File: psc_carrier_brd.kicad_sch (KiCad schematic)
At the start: 9 parts, among them J1 1731130154, J2 0836149012, J5 39301022, J6 6469028-1

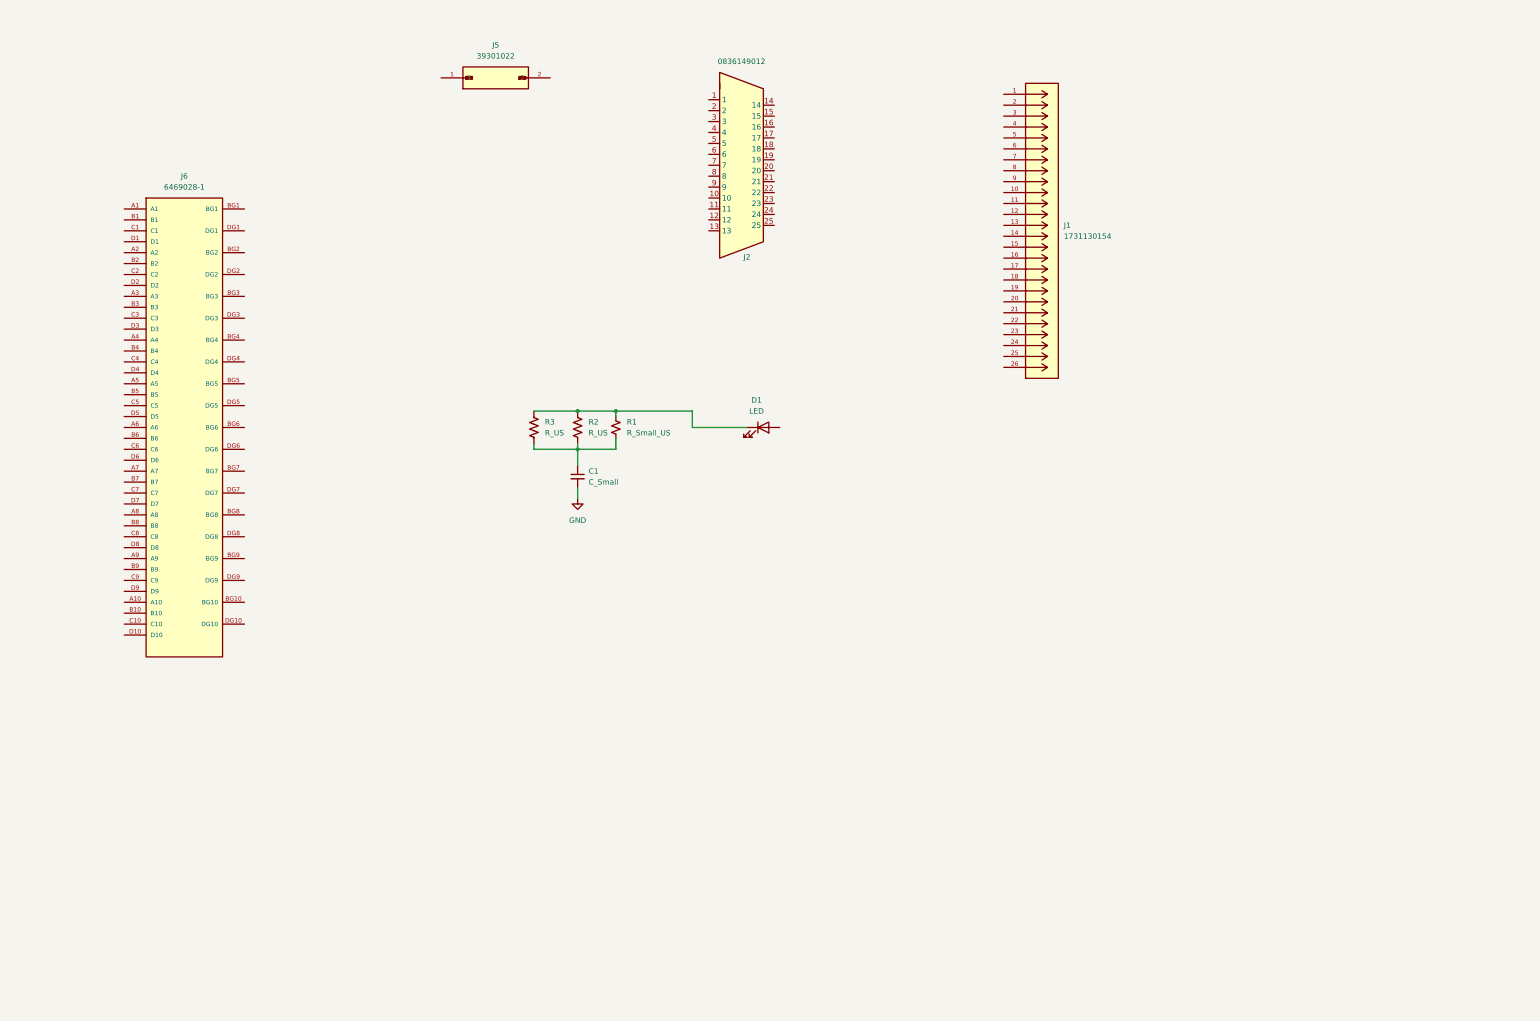
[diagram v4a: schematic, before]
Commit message: Upgrade to KiCad 9.  Add all I/O connectors
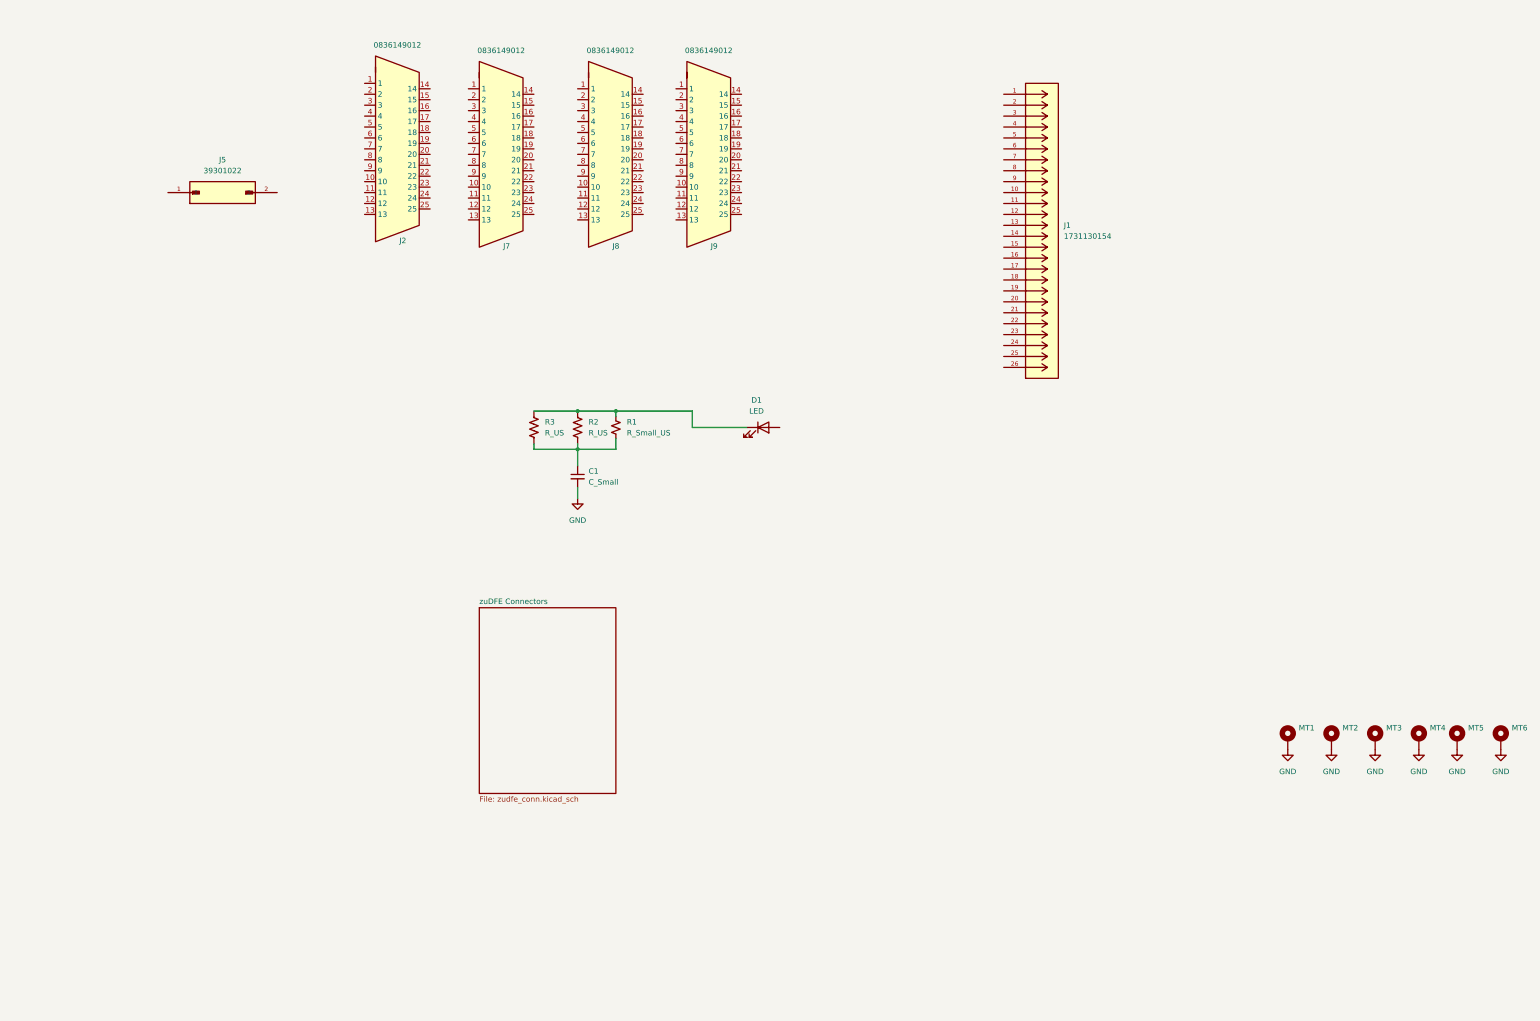
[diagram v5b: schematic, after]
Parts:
- removed J6: 6469028-1, myparts:TE_6469028-1, symbol 6469028-1:6469028-1
- added J7, J8, J9: 0836149012, myparts:0836149012, symbol 0836149012:0836149012
- added MT1, MT2, MT3, MT4, MT5, MT6: MountingHole_Pad, MountingHole:MountingHole_4.3mm_M4_DIN965_Pad, symbol Mechanical:MountingHole_Pad
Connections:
- net GND: now also MT1.1, MT2.1, MT3.1, MT4.1, MT5.1, MT6.1
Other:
- added sheet zuDFE Connectors (zudfe_conn.kicad_sch)
- moved on the sheet: J2, J5

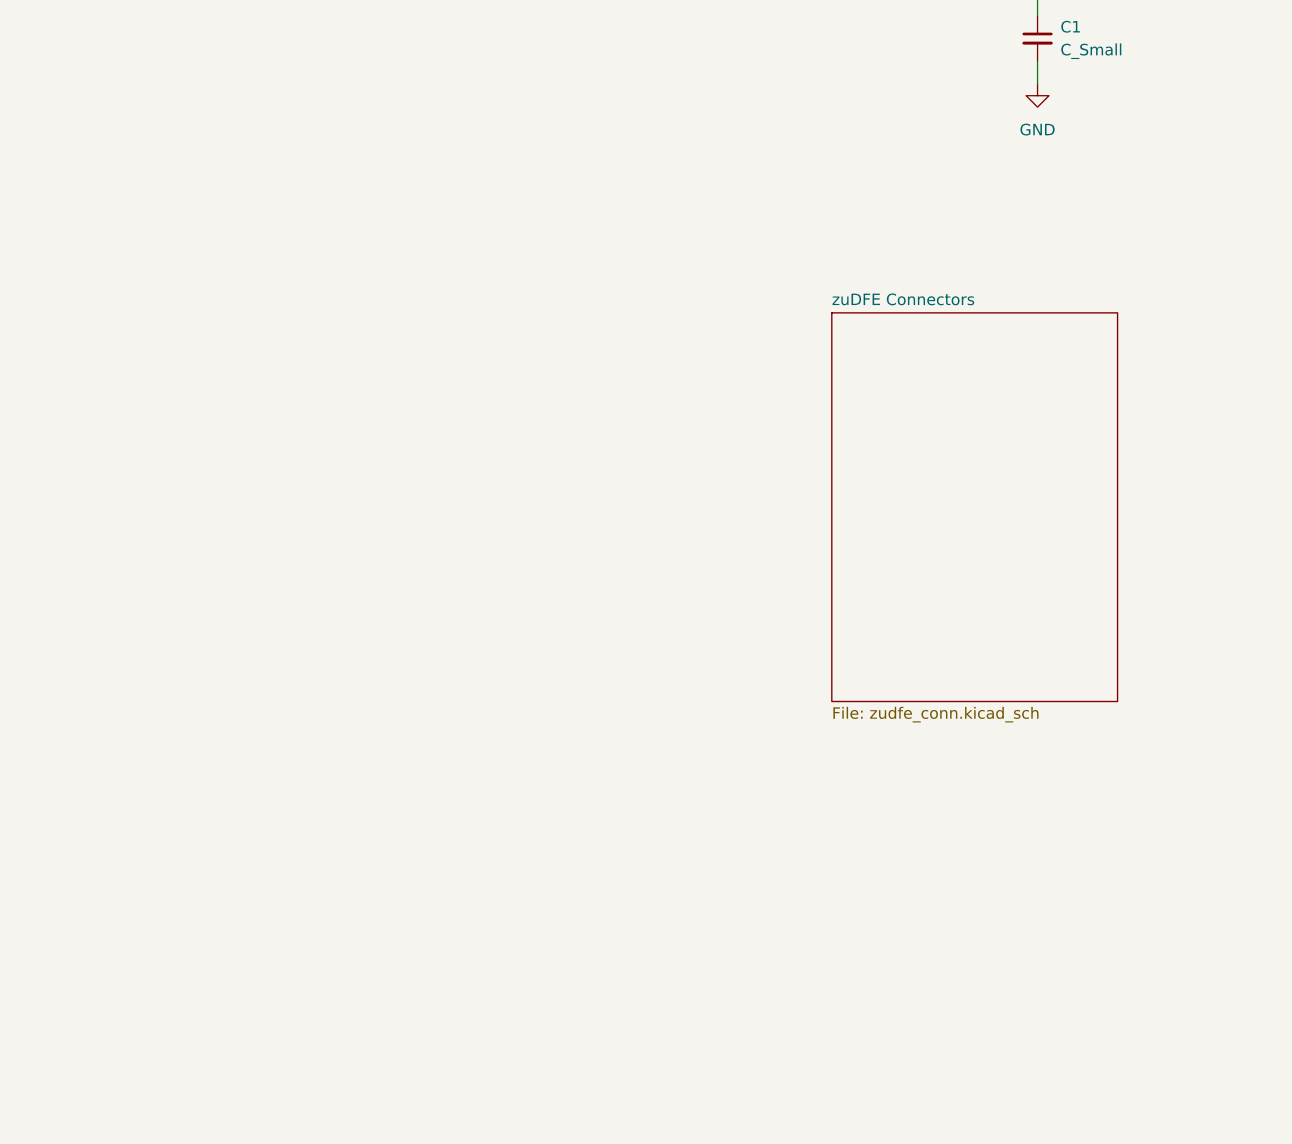
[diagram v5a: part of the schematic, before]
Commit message: Add DAC schematic page
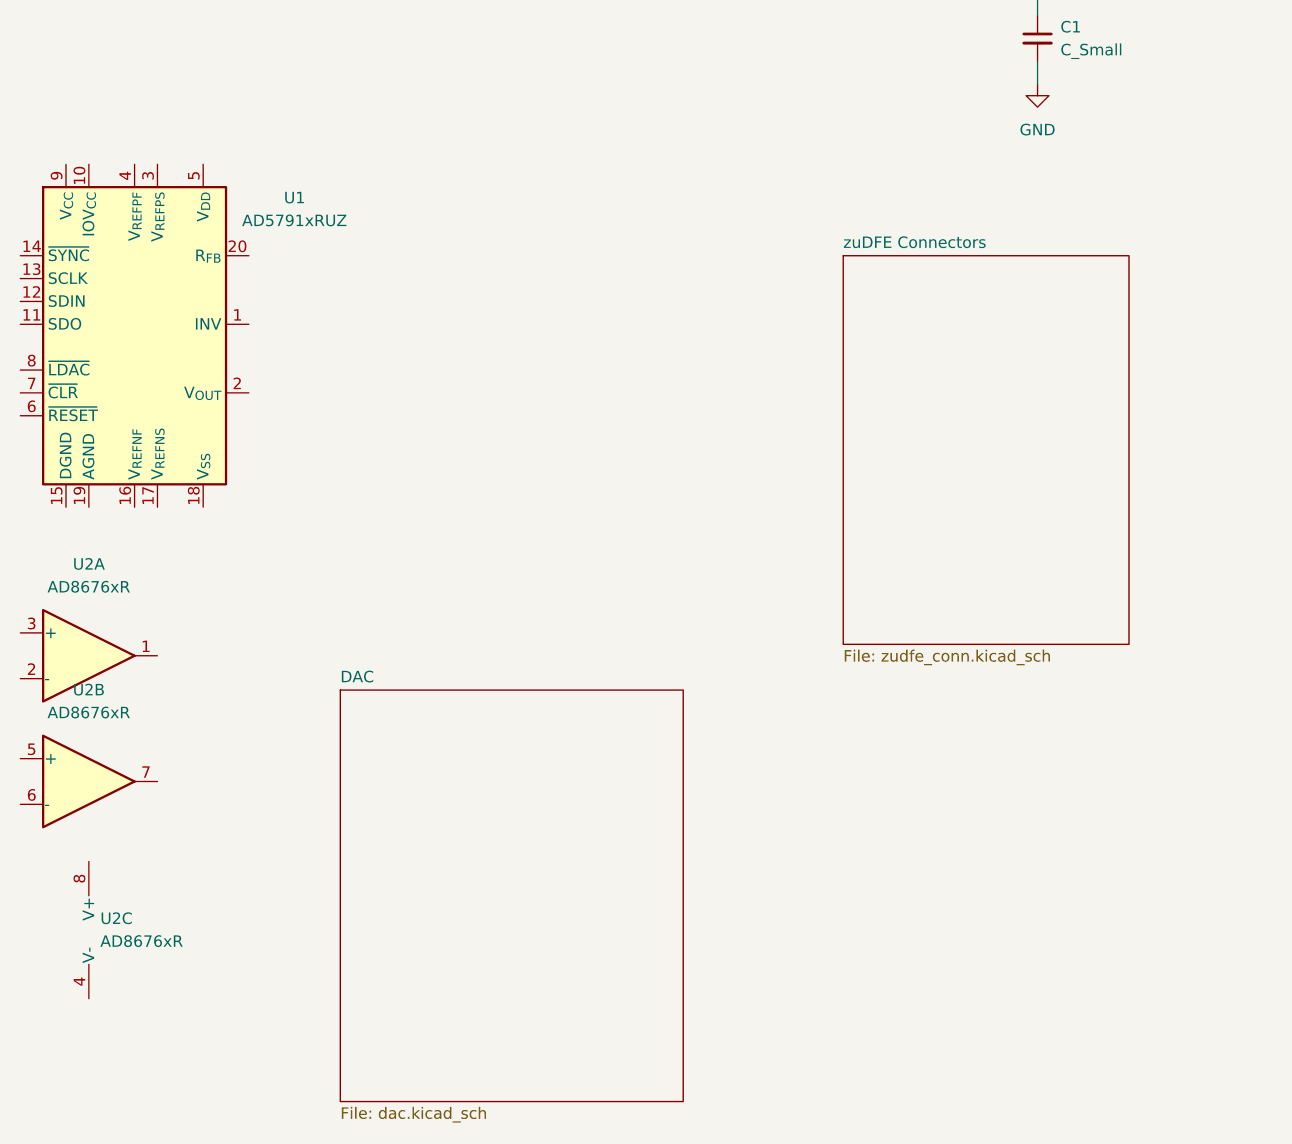
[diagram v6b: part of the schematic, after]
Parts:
- added U1: AD5791xRUZ, Package_SO:TSSOP-20_4.4x6.5mm_P0.65mm, symbol Analog_DAC:AD5791xRUZ
- added U2: AD8676xR, Package_SO:SOIC-8_3.9x4.9mm_P1.27mm, symbol Amplifier_Operational:AD8676xR
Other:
- added sheet DAC (dac.kicad_sch)

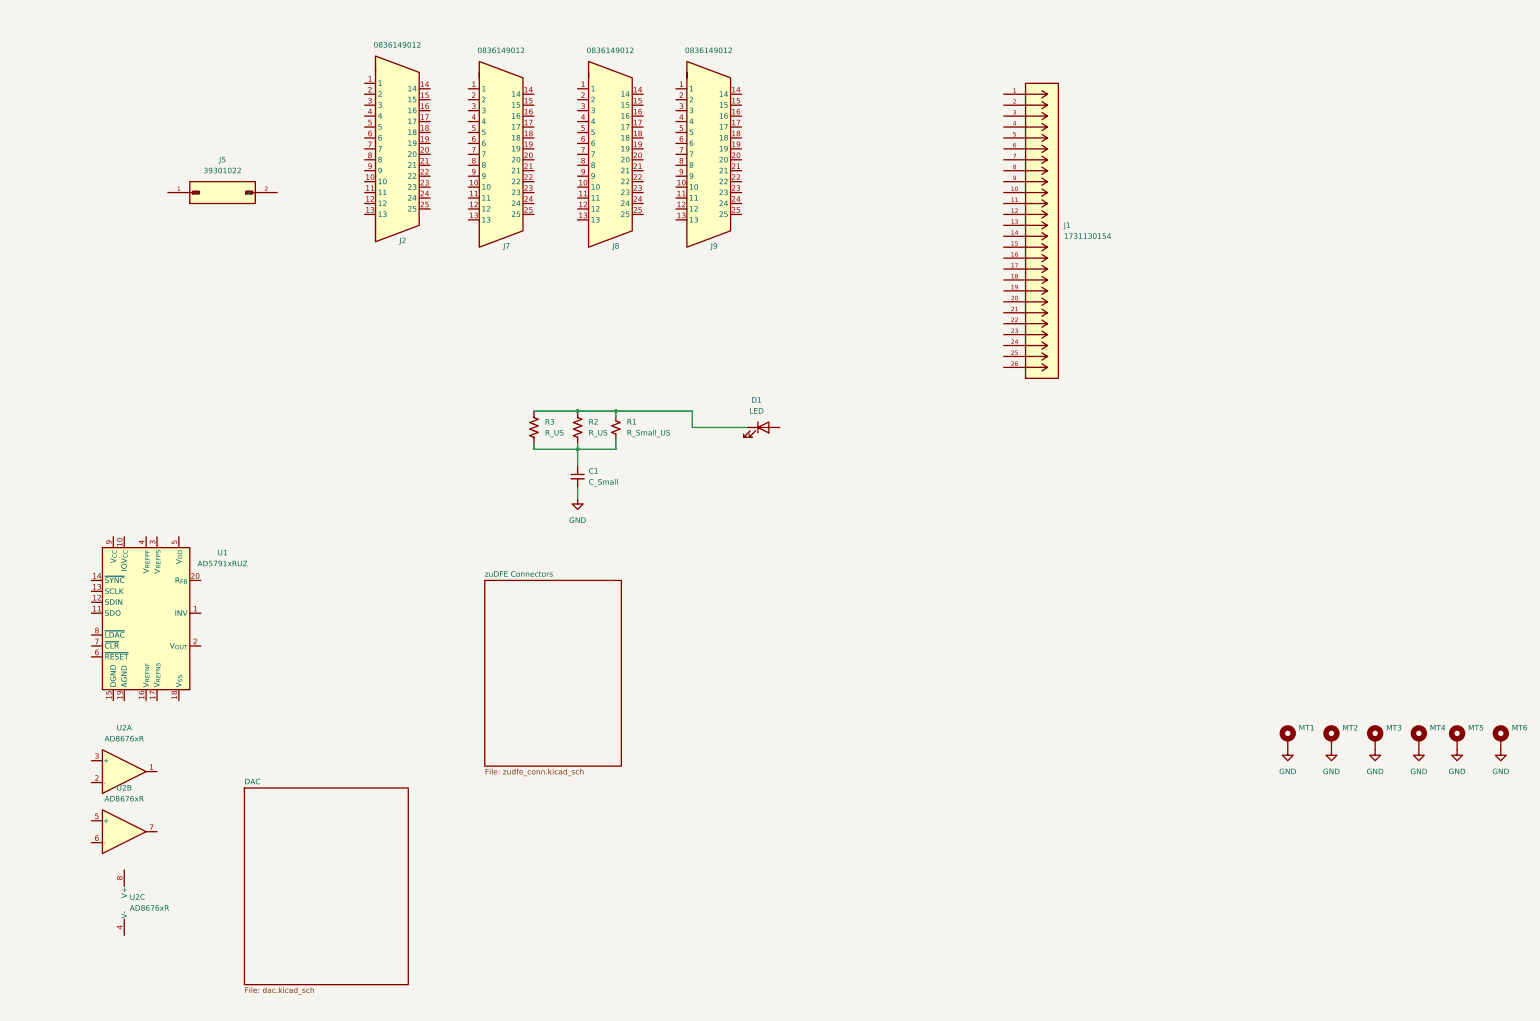
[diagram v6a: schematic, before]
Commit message: finish up regulator section
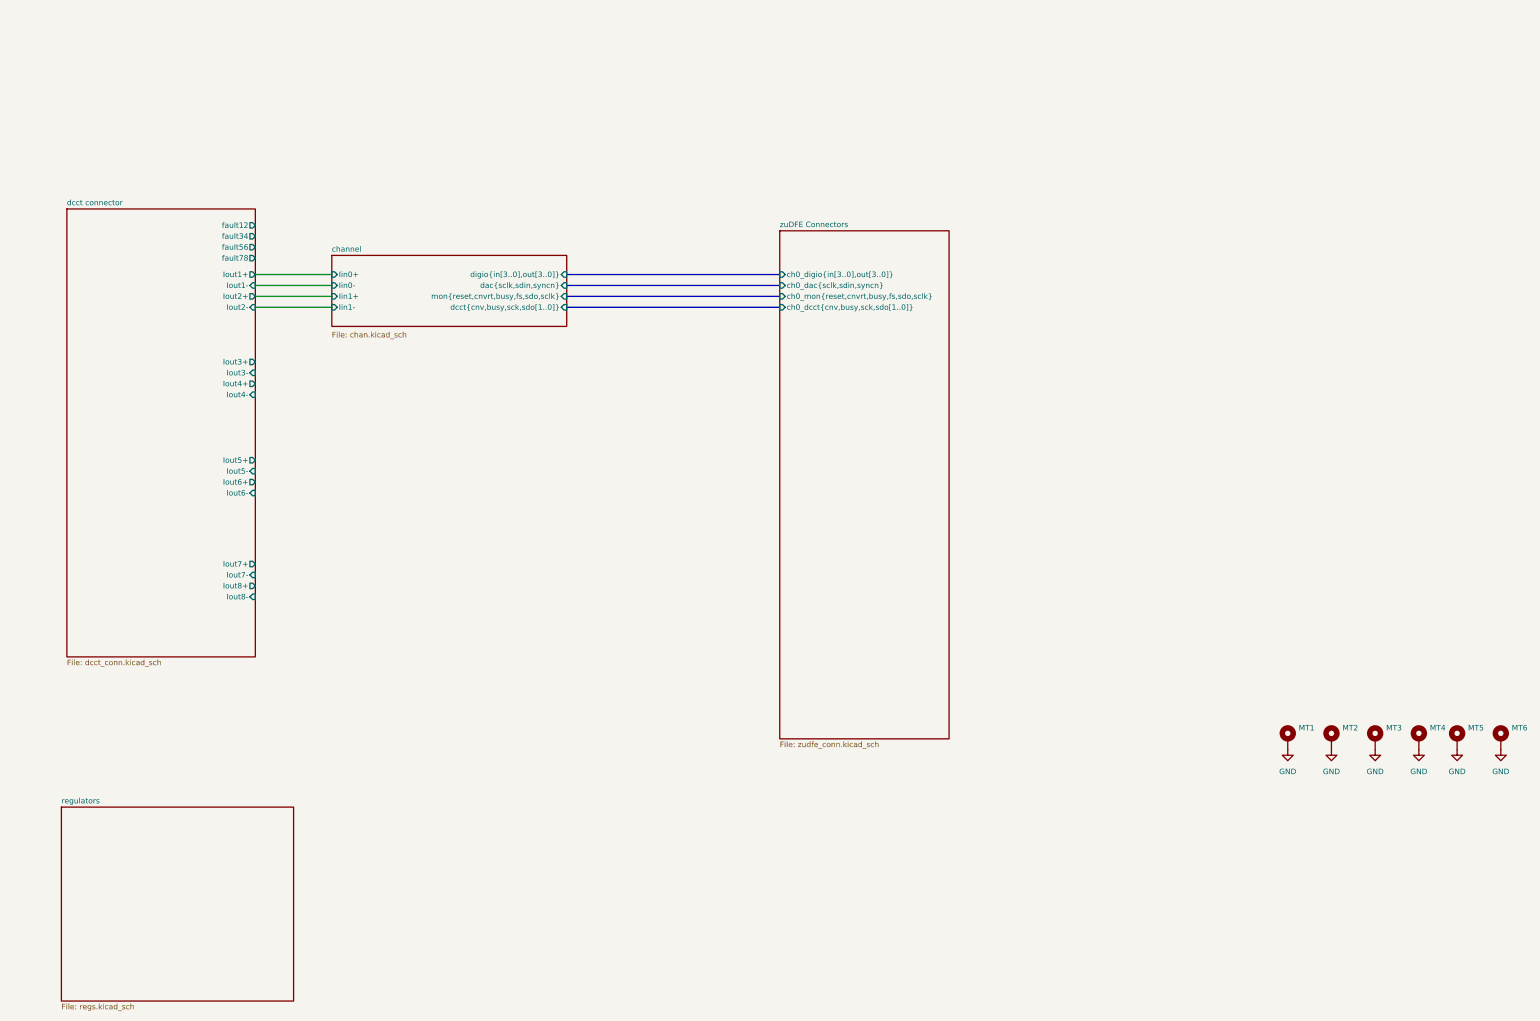
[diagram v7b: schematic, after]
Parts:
- removed C1: C_Small, Capacitor_SMD:C_0402_1005Metric, symbol Device:C_Small
- removed D1: LED, LED_SMD:LED_0603_1608Metric, symbol Device:LED
- removed J1: 1731130154, myparts:CONN_F15-26P135G0-5979_MOL, symbol 1731130154:1731130154
- removed J2, J7, J8, J9: 0836149012, myparts:0836149012, symbol 0836149012:0836149012
- removed J5: 39301022, myparts:MOLEX_39301022, symbol 39301022:39301022
- removed R1: R_Small_US, Resistor_SMD:R_0402_1005Metric, symbol Device:R_Small_US
- removed R2, R3: R_US, Resistor_SMD:R_0402_1005Metric, symbol Device:R_US
- removed U1: AD5791xRUZ, Package_SO:TSSOP-20_4.4x6.5mm_P0.65mm, symbol Analog_DAC:AD5791xRUZ
- removed U2: AD8676xR, Package_SO:SOIC-8_3.9x4.9mm_P1.27mm, symbol Amplifier_Operational:AD8676xR
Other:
- removed sheet DAC
- added sheet channel (chan.kicad_sch)
- added sheet dcct connector (dcct_conn.kicad_sch)
- added sheet regulators (regs.kicad_sch)
- sheet zuDFE Connectors ports: added ch0_dac{sclk,sdin,syncn}, ch0_dcct{cnv,busy,sck,sdo[1..0]}, ch0_digio{in[3..0],out[3..0]}, ch0_mon{reset,cnvrt,busy,fs,sdo,sclk}; removed none
